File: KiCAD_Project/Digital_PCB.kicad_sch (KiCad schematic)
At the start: 46 parts, among them J1 NP_Conn_01x02_Relief, J2 Board to Board, J3 NP_Conn_01x04_Relief, J4 1-0001205, J5 NP_Conn_01x04, J6 NP_Conn_01x02_Relief, J7 NP_Conn_01x04, U1 1-0000207, Y1 1-0000721

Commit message: Issue #2 (NP on all XBEE parts, J3 changed to SMPL)
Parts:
- removed J3: NP_Conn_01x04_Relief, np_connectors:SolderWire_1x04_Relief, symbol np_connectors:NP_Conn_01x04_Relief
- added J3: 1-0001156, connectors:1-0001156, symbol connectors:1-0001156
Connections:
- net +BATT: now also J3.4 (Pin_4)
- net GND: now also J3.1 (Pin_1)
- net Radio_RX: now also J3.2 (Pin_2)
- net Radio_TX: now also J3.3 (Pin_3)
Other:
- note added: "External Radio"
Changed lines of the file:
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@@
 (kicad_sch
-	(version 20231120)
+	(version 20250114)
 	(generator "eeschema")
-	(generator_version "8.0")
+	(generator_version "9.0")
 	(paper "USLetter")
 	(title_block
@@
 		(comment 3 "23830 West AR Highway 12")
 	)
+	(text "External Radio"
+		(exclude_from_sim no)
+		(at 16.764 73.66 90)
+		(effects
+			(font
+				(size 1.27 1.27)
+			)
+		)
+	)
+	(text "Default: 3-2"
+		(exclude_from_sim no)
+		(at 194.31 120.015 0)
+		(effects
+			(font
+				(size 1.27 1.27)
+			)
+			(justify right bottom)
+		)
+	)
+	(text "Default: 1-2"
+		(exclude_from_sim no)
+		(at 85.725 111.125 0)
+		(effects
+			(font
+				(size 1.27 1.27)
+			)
+			(justify left bottom)
+		)
+	)
+	(text "Default: 3-2"
+		(exclude_from_sim no)
+		(at 194.31 99.695 0)
+		(effects
+			(font
+				(size 1.27 1.27)
+			)
+			(justify right bottom)
+		)
+	)
+	(text "Default: 1-2"
+		(exclude_from_sim no)
+		(at 194.31 109.855 0)
+		(effects
+			(font
+				(size 1.27 1.27)
+			)
+			(justify right bottom)
+		)
+	)
+	(text "Default: 3-2"
+		(exclude_from_sim no)
+		(at 85.725 120.015 0)
+		(effects
+			(font
+				(size 1.27 1.27)
+			)
+			(justify left bottom)
+		)
+	)
+	(text "Default: 1-2"
+		(exclude_from_sim no)
+		(at 194.31 89.535 0)
+		(effects
+			(font
+				(size 1.27 1.27)
+			)
+			(justify right bottom)
+		)
+	)
 	(junction
 		(at 137.16 41.275)
@@
 			"k+laF+QKAAACk4RocfgOqvQNL0QGAgBALBISrQq3Gf9cET3hHgAAgBRFq0KdQywM0CoAAEiHpEWr"
 			"wlMS2zYCpOUFAABAIA/RErCspStTZQSHUAEAQMpkKVoyQuk2TeD0AwCAvPh/UbNVz/ggVM8AAAAA"
-			"SUVORK5CYII="
-		)
-	)
-	(text "Default: 3-2"
-		(exclude_from_sim no)
-		(at 194.31 120.015 0)
-		(effects
-			(font
-				(size 1.27 1.27)
-			)
-			(justify right bottom)
-		)
-	)
-	(text "Default: 1-2"
-		(exclude_from_sim no)
-		(at 85.725 111.125 0)
-		(effects
-			(font
-				(size 1.27 1.27)
-			)
-			(justify left bottom)
-		)
-	)
-	(text "Default: 3-2"
-		(exclude_from_sim no)
-		(at 194.31 99.695 0)
-		(effects
-			(font
-				(size 1.27 1.27)
-			)
-			(justify right bottom)
-		)
-	)
-	(text "Default: 1-2"
-		(exclude_from_sim no)
-		(at 194.31 109.855 0)
-		(effects
-			(font
-				(size 1.27 1.27)
-			)
-			(justify right bottom)
-		)
-	)
-	(text "Default: 3-2"
-		(exclude_from_sim no)
-		(at 85.725 120.015 0)
-		(effects
-			(font
-				(size 1.27 1.27)
-			)
-			(justify left bottom)
-		)
-	)
-	(text "Default: 1-2"
-		(exclude_from_sim no)
-		(at 194.31 89.535 0)
-		(effects
-			(font
-				(size 1.27 1.27)
-			)
-			(justify right bottom)
+			"SUVORK5CYIIAAAAAAAAAAAAAAAAAAAAAAAAAAAAAAAAAAAAAAAAAAAAAAAAAAAAAAAAAAAAAAAAA"
+			"AAAAAAAAAAAAAAAAAAAAAAAAAAAAAAAAAAAAAAAAAAAAAAAAAAAAAAAAAAAAAAAAAAAAAAAAAAAA"
+			"AAAAAAAAAAAAAAAAAAAAAAAAAAAAAAAAAAAAAAAAAAAAAAAAAAAAAAAAAAAAAAAAAAAAAAAAAAAA"
+			"AAAAAAAAAAAAAAAAAAAAAAAAAAAAAAAAAAAAAAAAAAAAAAAAAAAAAAAAAAAAAAAAAAAAAAAAAAAA"
+			"AAAAAAAAAAAAAAAAAAAAAAAAAAAAAAAAAAAAAAAAAAAAAAAAAAAAAAAAAAAAAAAAAAAAAAAAAAAA"
+			"AAAAAAAAAAAAAAAAAAAAAAAAAAAAAAAAAAAAAAAAAAAAAAAAAAAAAAAAAAAAAAAAAAAAAAAAAAAA"
+			"AAAAAAAAAAAAAAAAAAAAAAAAAAAAAAAAAAAAAAAAAAAAAAAAAAAAAAAAAAAAAAAAAAAAAAAAAAAA"
+			"AAAAAAAAAAAAAAAAAAAAAAAAAAAAAAAAAAAAAAAAAAAAAAAAAAAAAAAAAAAAAAAAAAAAAAAAAAAA"
+			"AAAAAAAAAAAAAAAAAAAAAAAAAAAAAAAAAAAAAAAAAAAAAAAAAAAAAAAAAAAAAAAAAAAAAAAAAAAA"
+			"AAAAAAAAAAAAAAAAAAAAAAAAAAAAAAAAAAAAAAAAAAAAAAAAAAAAAAAAAAAAAAAAAAAAAAAAAAAA"
+			"AAAAAAAAAAAAAAAAAAAAAAAAAAAAAAAAAAAAAAAAAAAAAAAAAAAAAAAAAAAAAAAAAAAAAAAAAAAA"
+			"AAAAAAAAAAAAAAAAAAAAAAAAAAAAAAAAAAAAAAAAAAAAAAAAAAAAAAAAAAAAAAAAAAAAAAAAAAAA"
+			"AAAAAAAAAAAAAAAAAAAAAAAAAAAAAAAAAAAAAAAAAAAAAAAAAAAAAAAAAAAAAAAAAAAAAAAAAAAA"
+			"AAAAAAAAAAAAAAAAAAAAAAAAAAAAAAAAAAAAAAAAAAAAAAAAAAAAAAAAAAAAAAAAAAAAAAAAAAAA"
+			"AAAAAAAAAAAAAAAAAAAAAAAAAAAAAAAAAAAAAAAAAAAAAAAAAAAAAAAAAAAAAAAAAAAAAAAAAAAA"
+			"AAAAAAAAAAAAAAAAAAAAAAAAAAAAAAAAAAAAAAAAAAAAAAAAAAAAAAAAAAAAAAAAAAAAAAAAAAAA"
+			"AAAAAAAAAAAAAAAAAAAAAAAAAAAAAAAAAAAAAAAAAAAAAAAAAAAAAAAAAAAAAAAAAAAAAAAAAAAA"
+			"AAAAAAAAAAAAAAAAAAAAAAAAAAAAAAAAAAAAAAAAAAAAAAAAAAAAAAAAAAAAAAAAAAAAAAAAAAAA"
+			"AAAAAAAAAA=="
 		)
 	)
@@
 	)
 	(symbol
-		(lib_id "np_connectors:NP_Conn_01x04_Relief")
-		(at 19.05 74.93 180)
-		(unit 1)
-		(exclude_from_sim no)
-		(in_bom yes)
-		(on_board yes)
-		(dnp no)
-		(property "Reference" "J3"
-			(at 19.05 67.31 0)
-			(effects
-				(font
-					(size 1.27 1.27)
-				)
-			)
-		)
-		(property "Value" "NP_Conn_01x04_Relief"
-			(at 19.05 67.31 0)
-			(effects
-				(font
-					(size 1.27 1.27)
-				)
-				(hide yes)
-			)
-		)
-		(property "Footprint" "np_connectors:SolderWire_1x04_Relief"
-			(at 19.05 74.93 0)
-			(effects
-				(font
-					(size 1.27 1.27)
-				)
-				(hide yes)
-			)
-		)
-		(property "Datasheet" "~"
-			(at 19.05 74.93 0)
-			(effects
-				(font
-					(size 1.27 1.27)
-				)
-				(hide yes)
-			)
-		)
-		(property "Description" ""
-			(at 19.05 74.93 0)
-			(effects
-				(font
-					(size 1.27 1.27)
-				)
-				(hide yes)
-			)
-		)
-		(property "Internal Part Number" "0-0000000"
-			(at 19.05 74.93 0)
-			(effects
-				(font
-					(size 1.27 1.27)
-				)
-				(hide yes)
-			)
-		)
-		(property "Populated" "0"
-			(at 19.05 74.93 0)
-			(effects
-				(font
-					(size 1.27 1.27)
-				)
-				(hide yes)
-			)
-		)
-		(property "PValue" "External Radio"
-			(at 16.51 73.66 90)
-			(effects
-				(font
-					(size 1.27 1.27)
-				)
-			)
-		)
-		(pin "1"
-		)
-		(pin "2"
-		)
-		(pin "3"
-		)
-		(pin "4"
-		)
-		(instances
-			(project "Digital_PCB"
-				(path "/3dbf31f8-25b6-4bae-a8a1-93cabd4e019f"
-					(reference "J3")
-					(unit 1)
-				)
-			)
-		)
-	)
-	(symbol
 		(lib_id "power:+3V3")
 		(at 213.36 133.35 0)
@@
 	)
 	(symbol
+		(lib_id "connectors:1-0001156")
+		(at 19.05 74.93 180)
+		(unit 1)
+		(exclude_from_sim no)
+		(in_bom yes)
+		(on_board yes)
+		(dnp no)
+		(property "Reference" "J3"
+			(at 19.05 67.564 0)
+			(effects
+				(font
+					(size 1.27 1.27)
+				)
+			)
+		)
+		(property "Value" "1-0001156"
+			(at 19.05 67.31 0)
+			(effects
+				(font
+					(size 1.27 1.27)
+				)
+				(hide yes)
+			)
+		)
+		(property "Footprint" "connectors:1-0001156"
+			(at 19.05 74.93 0)
+			(effects
+				(font
+					(size 1.27 1.27)
+				)
+				(hide yes)
+			)
+		)
+		(property "Datasheet" "~"
+			(at 19.05 74.93 0)
+			(effects
+				(font
+					(size 1.27 1.27)
+				)
+				(hide yes)
+			)
+		)
+		(property "Description" "Connector Header Through Hole 4 position 0.050\" (1.27mm)"
+			(at 19.05 74.93 0)
+			(effects
+				(font
+					(size 1.27 1.27)
+				)
+				(hide yes)
+			)
+		)
+		(property "Internal Part Number" "1-0001156"
+			(at 19.05 74.93 0)
+			(effects
+				(font
+					(size 1.27 1.27)
+				)
+				(hide yes)
+			)
+		)
+		(property "Populated" "1"
+			(at 19.05 74.93 0)
+			(effects
+				(font
+					(size 1.27 1.27)
+				)
+				(hide yes)
+			)
+		)
+		(property "PValue" "4 Pos"
+			(at 19.05 66.04 0)
+			(effects
+				(font
+					(size 1.27 1.27)
+				)
+				(hide yes)
+			)
+		)
+		(pin "1"
+		)
+		(pin "2"
+		)
+		(pin "4"
+		)
+		(pin "3"
+		)
+		(instances
+			(project ""
+				(path "/3dbf31f8-25b6-4bae-a8a1-93cabd4e019f"
+					(reference "J3")
+					(unit 1)
+				)
+			)
+		)
+	)
+	(symbol
 		(lib_id "capacitors_0603:1-0000007")
 		(at 147.32 48.26 270)
@@
 		(at 67.945 175.895)
 		(size 25.4 25.4)
+		(exclude_from_sim no)
+		(in_bom yes)
+		(on_board yes)
+		(dnp no)
 		(fields_autoplaced yes)
 		(stroke
@@
 		(at 94.615 175.895)
 		(size 25.4 25.4)
+		(exclude_from_sim no)
+		(in_bom yes)
+		(on_board yes)
+		(dnp no)
 		(fields_autoplaced yes)
 		(stroke
@@
 		(at 41.275 175.895)
 		(size 25.4 25.4)
+		(exclude_from_sim no)
+		(in_bom yes)
+		(on_board yes)
+		(dnp no)
 		(fields_autoplaced yes)
 		(stroke
@@
 		(at 14.605 175.895)
 		(size 25.4 25.4)
+		(exclude_from_sim no)
+		(in_bom yes)
+		(on_board yes)
+		(dnp no)
 		(fields_autoplaced yes)
 		(stroke
@@
 		)
 	)
+	(embedded_fonts no)
 )

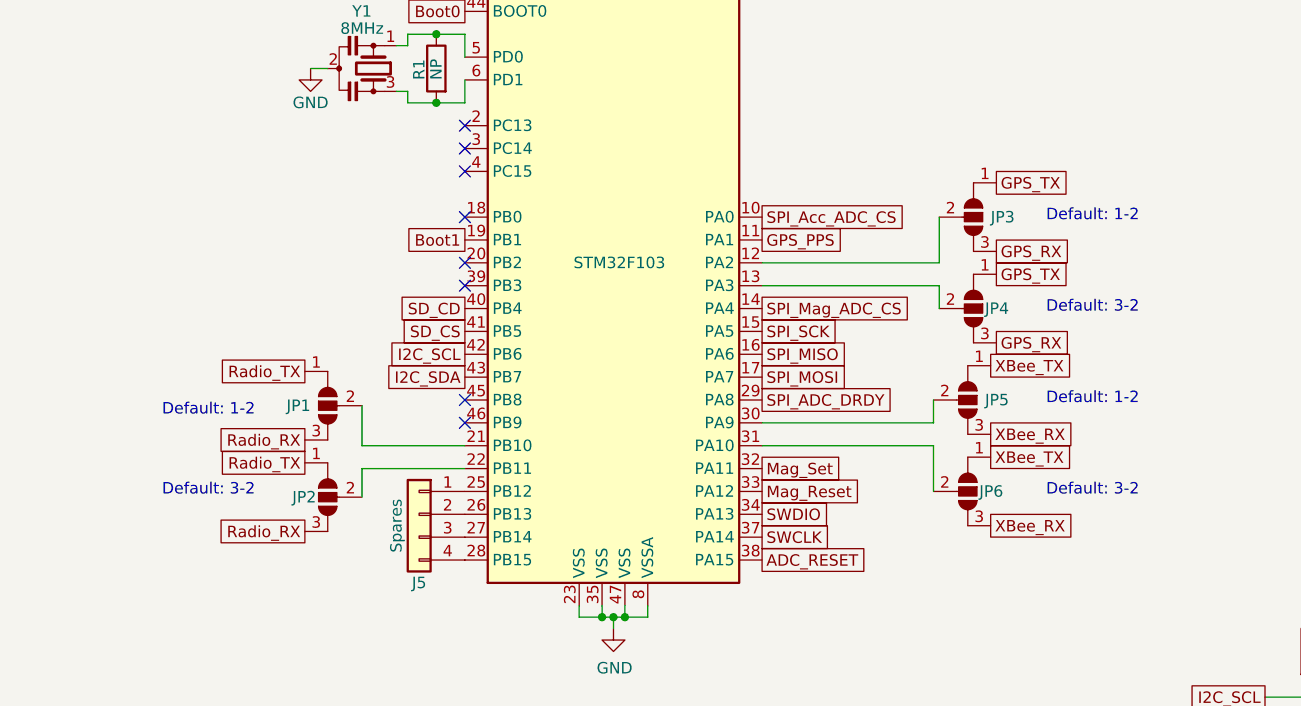
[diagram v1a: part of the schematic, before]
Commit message: Fixed issue #6 (Removed RX/TX Jumpers)
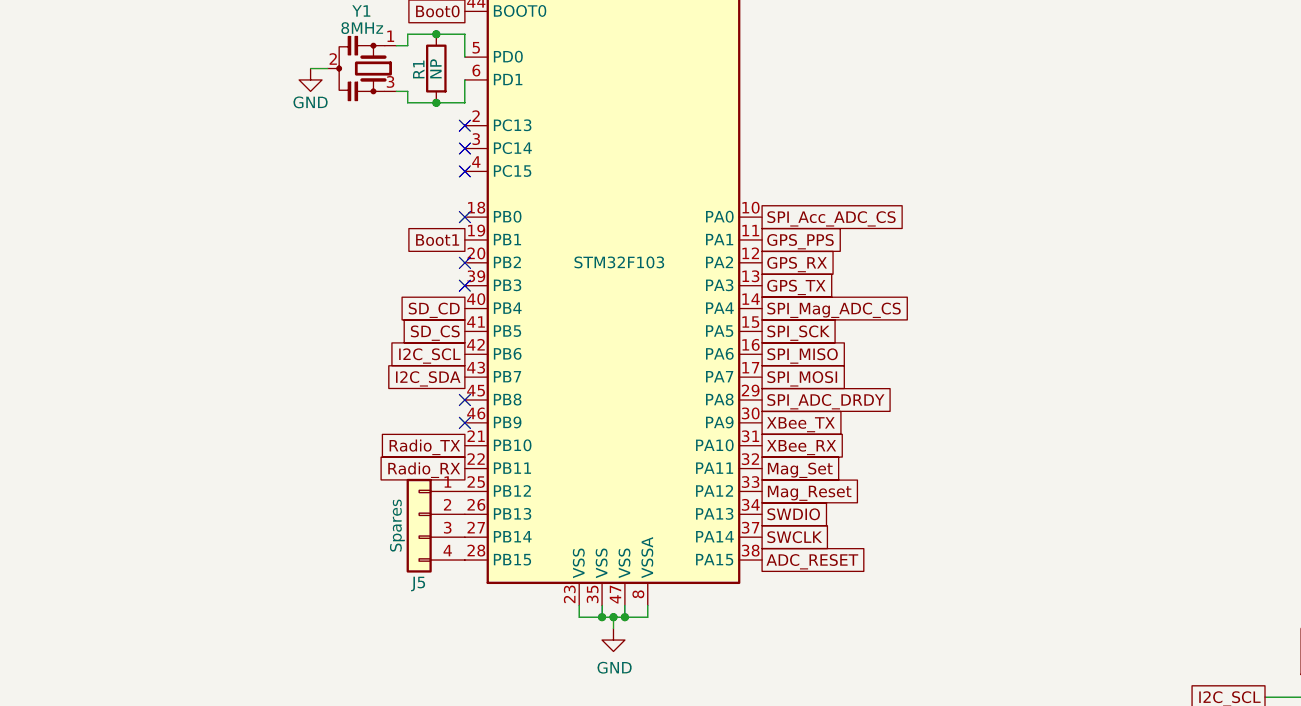
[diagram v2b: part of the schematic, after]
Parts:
- removed JP1, JP2, JP3, JP4, JP5, JP6: SolderJumper_3_Open, Jumper:SolderJumper-3_P1.3mm_Open_RoundedPad1.0x1.5mm_NumberLabels, symbol Jumper:SolderJumper_3_Open
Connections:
- net GPS_RX: now also U1.12 (PA2)
- net GPS_TX: now also U1.13 (PA3)
- net Radio_RX: now also U1.22 (PB11)
- net Radio_TX: now also U1.21 (PB10)
- net XBee_RX: now also U1.31 (PA10)
- net XBee_TX: now also U1.30 (PA9)
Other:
- note removed: "Default: 1-2"
- note removed: "Default: 3-2"

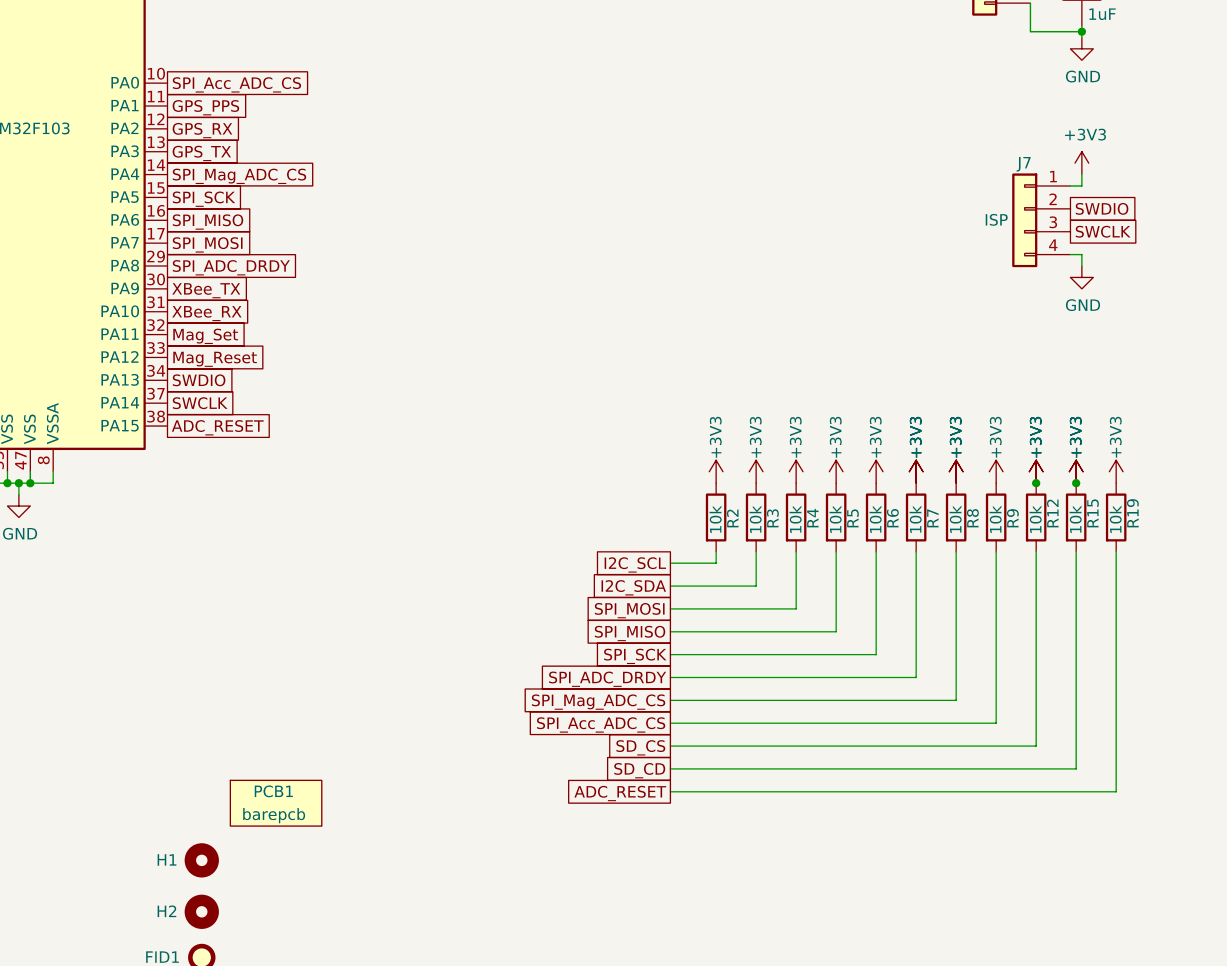
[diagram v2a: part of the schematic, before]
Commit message: Fixed Issue #3 (ADC Cleanup and Removed Second ADC/MAG Component)
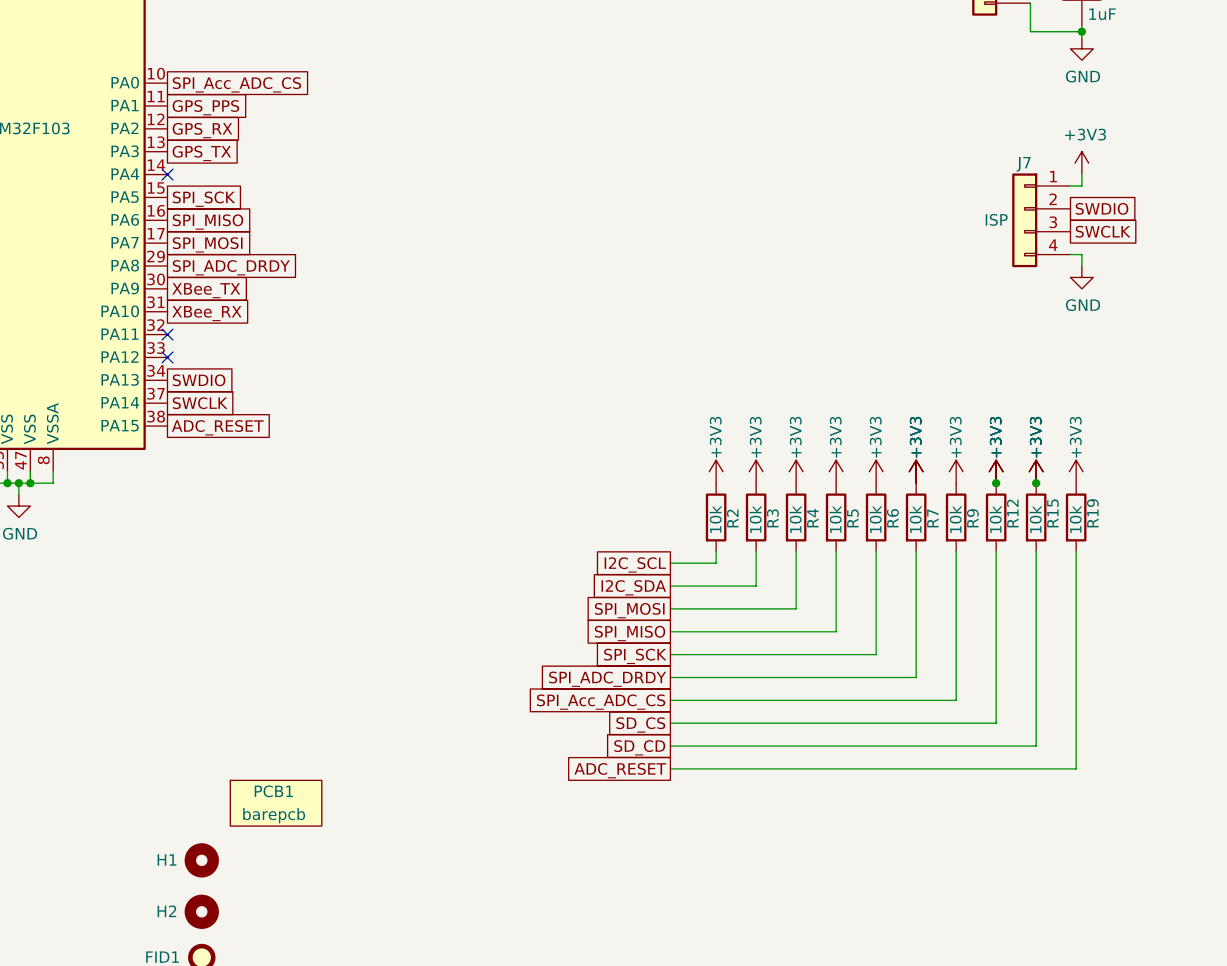
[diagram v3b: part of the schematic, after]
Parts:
- removed R8: 1-0000010, resistors_0603:1-0000010, symbol resistors_0603:1-0000010
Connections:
- net Mag_Reset: no longer names the net of U1.33 (PA12)
- net Mag_Set: no longer names the net of U1.32 (PA11)
- net SPI_Mag_ADC_CS: no longer names the net of U1.14 (PA4)
- no-connect marks 13 -> 16
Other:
- moved on the sheet: R12, R15, R19, R9

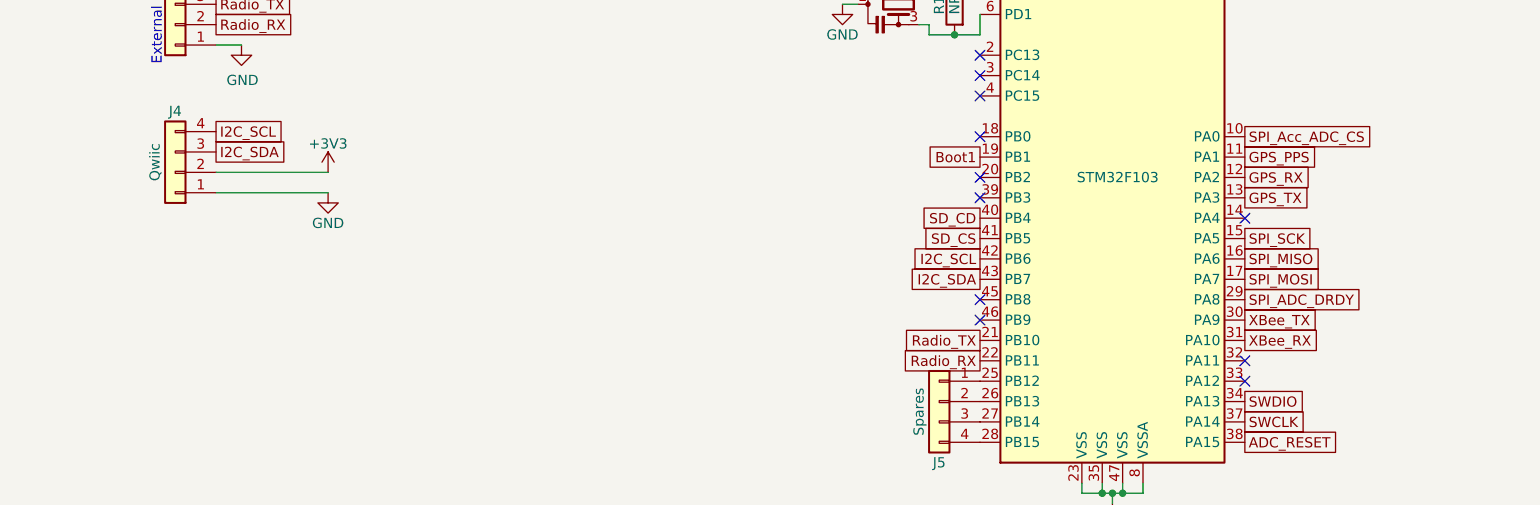
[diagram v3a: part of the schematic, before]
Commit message: Fixed Issue #1 (Added SMPL RGB Connector... NOTE: had to move the ADC DRDY pin to PA4 to get access to all required PWM Pins)
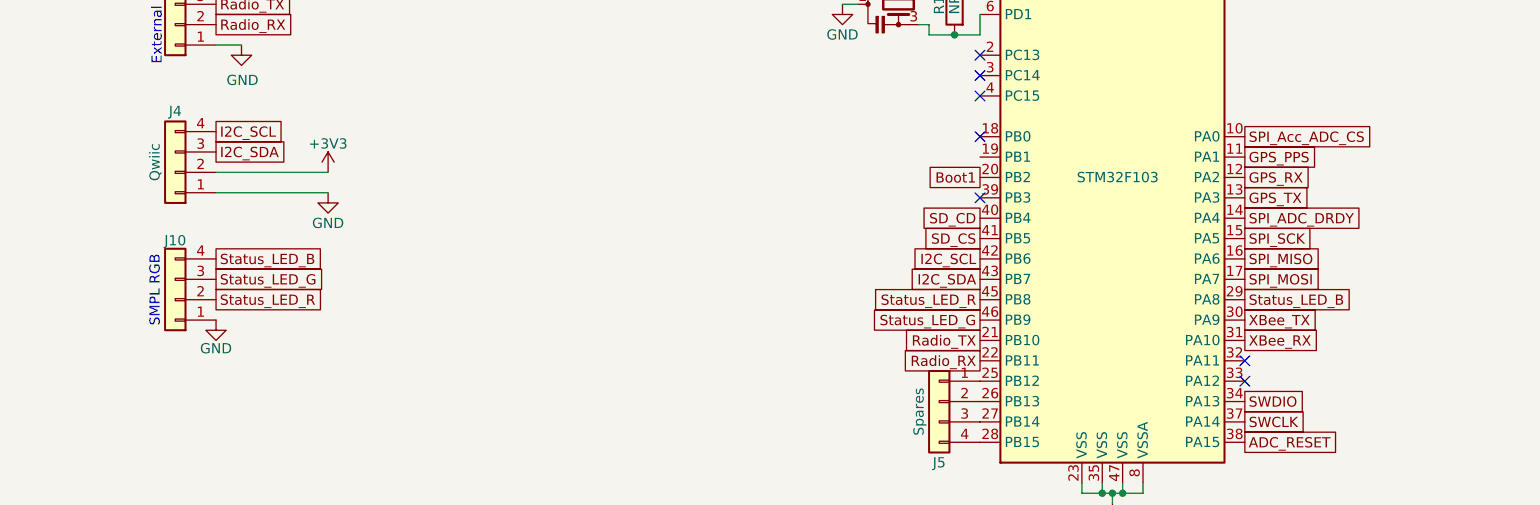
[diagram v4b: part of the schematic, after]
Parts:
- added J10: 1-0001156, connectors:1-0001156, symbol connectors:1-0001156
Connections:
- net Boot1: now also U1.20 (PB2); no longer U1.19 (PB1)
- net GND: now also J10.1 (Pin_1)
- net SPI_ADC_DRDY: now also U1.14 (PA4); no longer U1.29 (PA8)
- net Status_LED_R: now reaches U1.45 (PB8)
- net Status_LED_R: now also J10.2 (Pin_2)
- net Status_LED_G: now reaches U1.46 (PB9)
- net Status_LED_G: now also J10.3 (Pin_3)
- new net Status_LED_B: J10.4 (Pin_4), U1.29 (PA8)
- no-connect marks 16 -> 12
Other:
- note added: "SMPL RGB"
